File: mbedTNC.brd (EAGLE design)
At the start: 66.7 x 32.9 mm, 58 parts, among them IC1 MKL25ZXXVLH4, IC2 TPS61201, IC3 LMV321-SOT-23-5, J1 MAX5481ETE, J2 SS-7066-NF, Q2 MMBT2222A, Q3 8Mhz, SW3 SPST_TACT-KMR2, U1 BMP180, U2 MCP73831, U3 MAX2659ELT+T, U4 S25FL208K0RMFI013

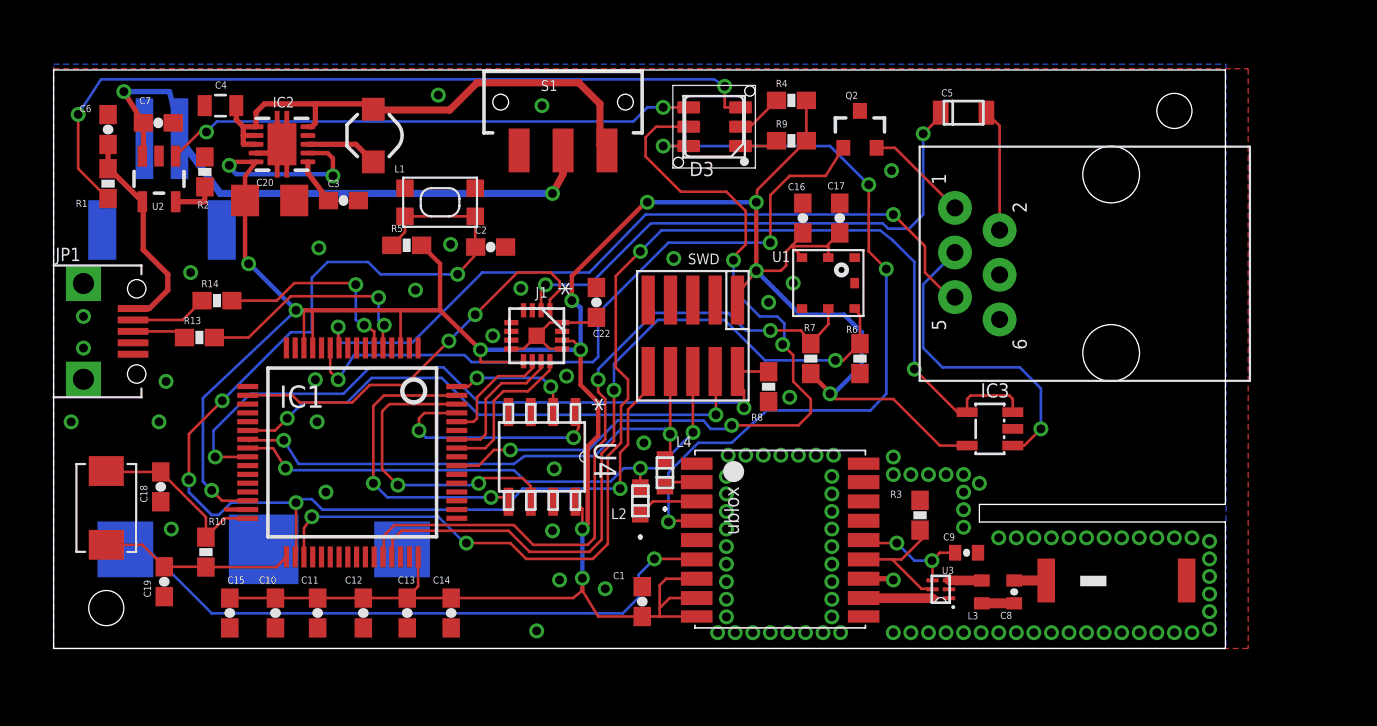
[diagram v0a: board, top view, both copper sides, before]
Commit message: Update
Added support for Yaesu/Icom radios. Moved components around.
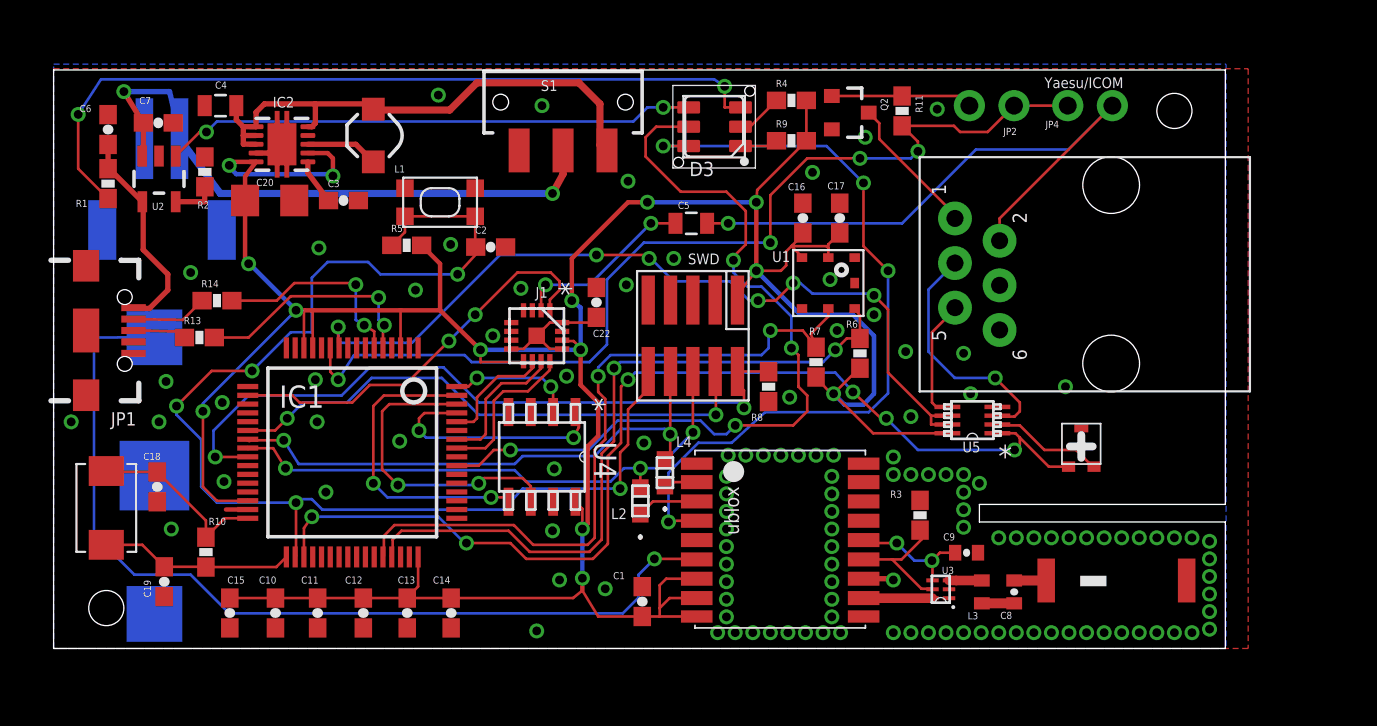
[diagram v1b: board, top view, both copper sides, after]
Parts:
- removed IC3: LMV321-SOT-23-5, dp_devices:SOT-23-5
- added JP2, JP4: JUMPER-PTH-2-NO, SparkFun-Passives:PTH-JUMPER-2-NO_NO_SILK
- added R11: 1K, SparkFun-Resistors:0603-RES
- added U$2: PVA2, wrea:PVA2
- added U5: LMV358, wrea:DDU8-M
- C5: value F921C105MPA -> 10uF; device wrea:PCAP87X53_47N_NIC -> SparkFun-Capacitors:0805
- JP1: value USB-RECEPTABLE -> USB_MICROB_PLUGCONN-11752; device daspilker:FCI-10103594-0001LF -> SparkFun-Connectors:USB-B-MICRO-SMD_V03
- moved C5 16.7 mm to (36.3, 24.2)
- moved BAT1 7.51 mm to (5.74, 9.84), turned to 270 degrees
- moved JP1 1.85 mm to (1.85, 18.1), turned to 0 degrees
- moved Q2 1.17 mm to (45.3, 30.5), turned to 270 degrees
- moved J2 0.60 mm to (58.7, 21.3)
- moved R7 0.36 mm to (43.4, 16.3)
- moved R6 0.30 mm to (45.9, 16.8)
- moved C18 0.20 mm to (5.90, 9.20)
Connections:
- new net N$24: JP2.1, Q2.1, R11.1
- new net N$25: J2.5, U5.5
- new net N$26: U$2.2, U5.2
- net 3.3V: now also U5.8; no longer IC3.5
- net AUDIO_IN: now also U$2.1, U5.1; no longer IC3.3, IC3.4
- net AUDIO_OUT: now also JP4.2
- net CARRIER_IN: now also U5.6, U5.7; no longer J2.5
- net GND: now also JP1.GND1, Q2.2, U$2.3, U5.4; no longer IC3.2, JP1.5, Q2.3
- net N$1: now also JP1.D-1; no longer JP1.2
- net N$18: now also JP1.D+1; no longer JP1.3
- net N$22: now also U5.3; no longer IC3.1
- net N$3: now also Q2.3; no longer Q2.2
- net N$6: now also JP1.VBUS1; no longer JP1.1
- net PTT: now also JP2.2, JP4.1, R11.2; no longer Q2.1
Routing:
- net AUDIO_OUT: track 7.00 -> 36.2 mm, vias 0 -> 1
- net N$21: track 31.2 -> 10.4 mm
- net N$5: track 36.1 -> 52.9 mm
- net PTT: track 40.0 -> 56.7 mm, vias 2 -> 4
- net AUDIO_IN: track 69.8 -> 60.1 mm, vias 4 -> 6
- net N$24: track 0.00 -> 8.06 mm
- net N$25: track 0.00 -> 6.92 mm
- net N$26: track 0.00 -> 6.50 mm
- net N$22: track 18.1 -> 14.0 mm
- net CARRIER_IN: track 43.1 -> 47.0 mm, vias 2 -> 6
- net 3.3V: track 181.0 -> 184.5 mm
- net SDA: track 42.7 -> 40.5 mm
- net N$3: track 5.88 -> 8.05 mm
- net NRESET: track 71.1 -> 71.9 mm
- net GND: vias 109 -> 120
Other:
- board text added: "Yaesu/ICOM"

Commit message: Update
Changed to a 2 circuit digipot. Various other changes
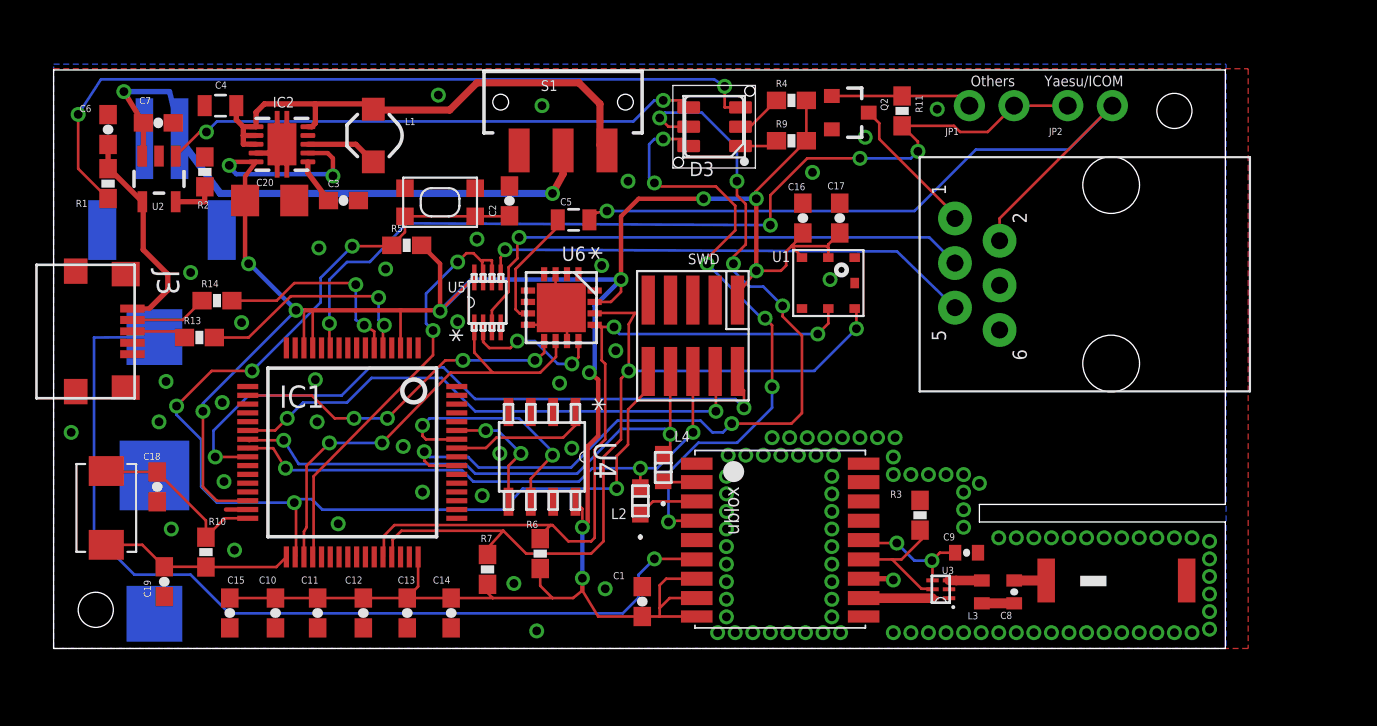
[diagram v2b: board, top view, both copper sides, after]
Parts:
- removed C22: 0.1uF, SparkFun-Capacitors:0603-CAP
- removed J1: MAX5481ETE, wrea:21-0136I_T1633F-3
- removed JP4: JUMPER-PTH-2-NO, SparkFun-Passives:PTH-JUMPER-2-NO_NO_SILK
- removed R8: 10k, SparkFun-Resistors:0603-RES
- removed U$2: PVA2, wrea:PVA2
- added J3: 1981568-1, wrea:CONN_1981568-1
- added U6: MCP4661-XXXX_ML, wrea:QFN16_4X4MC
- JP1: value USB_MICROB_PLUGCONN-11752 -> JUMPER-PTH-2-NO; device SparkFun-Connectors:USB-B-MICRO-SMD_V03 -> SparkFun-Passives:PTH-JUMPER-2-NO_NO_SILK
- R6, R7: value 4.7K -> 2.2k
- moved JP1 53.1 mm to (53.4, 30.9)
- moved U5 28.4 mm to (24.7, 19.7), turned to 90 degrees
- moved R7 22.1 mm to (24.7, 4.50)
- moved R6 21.5 mm to (27.7, 5.40)
- moved C5 6.70 mm to (29.6, 24.4)
- moved JP2 5.60 mm to (59.0, 30.9)
- moved C2 2.84 mm to (25.9, 25.5), turned to 90 degrees
- moved L4 0.32 mm to (34.7, 10.3)
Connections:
- removed net N$19: C22.1, J1.13, J1.16, J1.17, J1.8
- removed net N$26: U$2.2, U5.2
- removed net SPI1_MISO: IC1.64, U4.2
- removed net SPI1_MOSI: IC1.63, U4.5
- removed net SPI1_PCS0: IC1.61, U4.1
- removed net SPI1_SCK: IC1.62, U4.6
- new net P1W: U5.2, U6.6
- net 3.3V: now also U6.15; no longer J1.14, J1.9
- net AUDIO_IN: now also U6.7; no longer U$2.1
- net AUDIO_OUT: now also JP2.2; no longer JP4.2
- net CARRIER_IN: now also IC1.36; no longer IC1.10
- net DAC: now also U6.9; no longer J1.1
- net GND: now also J3.1, U6.10, U6.13, U6.14, U6.17, U6.3, U6.4, U6.5; no longer C22.2, J1.3, JP1.GND1, R8.2, U$2.3
- net N$1: now also J3.4; no longer JP1.D-1
- net N$18: now also J3.3; no longer JP1.D+1
- net N$21: now also U6.8; no longer J1.2
- net N$24: now also JP1.1; no longer JP2.1
- net N$6: now also J3.5; no longer JP1.VBUS1
- net PTT: now also JP1.2, JP2.1; no longer JP2.2, JP4.1
- net SCL: now also R6.1, U6.1; no longer R7.1
- net SDA: now also R7.1, U6.2; no longer R6.1
- net SPI0_MISO: now also U4.2; no longer IC1.60, J1.10
- net SPI0_MOSI: now also U4.5
- net SPI0_PCS0: now also U4.1; no longer J1.12
- net SPI0_SCK: now also U4.6; no longer J1.11
- net TMS: no longer R8.1
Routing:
- net AUDIO_IN: track 60.1 -> 25.9 mm, vias 6 -> 2
- net CARRIER_IN: track 47.0 -> 24.9 mm, vias 6 -> 2
- net N$25: track 6.92 -> 28.5 mm, vias 0 -> 1
- net 3.3V: track 184.5 -> 163.9 mm, vias 14 -> 13
- net SPI1_SCK: track 17.8 -> 0.00 mm, vias 2 -> 0
- net SPI1_MOSI: track 17.5 -> 0.00 mm, vias 2 -> 0
- net N$22: track 14.0 -> 31.1 mm
- net SPI1_PCS0: track 13.5 -> 0.00 mm, vias 2 -> 0
- net GPS_LED: track 45.0 -> 35.7 mm, vias 4 -> 6
- net P1W: track 0.00 -> 8.18 mm, vias 0 -> 2
- net N$19: track 7.53 -> 0.00 mm
- net SPI1_MISO: track 7.26 -> 0.00 mm, vias 2 -> 0
- net SPI0_MOSI: track 0.00 -> 7.23 mm, vias 0 -> 2
- net SDA: track 40.5 -> 47.3 mm
- net SPI0_MISO: track 6.67 -> 0.00 mm
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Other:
- board text added: "Others"

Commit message: Update.
Move to 4 layer board. New LNA with internal switch for an active
external ant. Finalizing parts, moved stuff around.
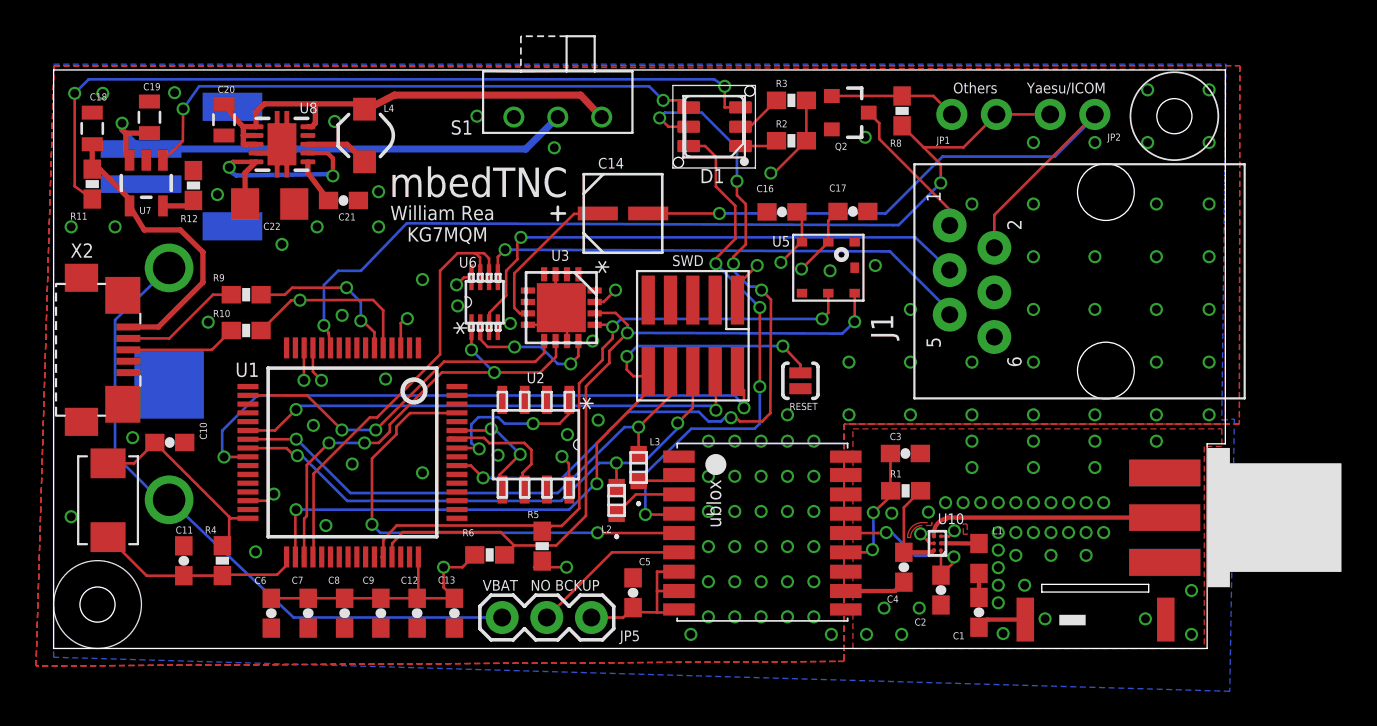
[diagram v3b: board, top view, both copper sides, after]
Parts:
- removed BAT1: (no value), SparkFun-Electromechanical:BATTCON_12MM
- removed C15: 1.0uF, SparkFun-Capacitors:0603-CAP
- removed IC1: MKL25ZXXVLH4, wrea:64-LQFP
- removed J2: SS-7066-NF, wrea:SS-7066-NF
- removed J3: 1981568-1, wrea:CONN_1981568-1
- removed JP3: LiPo Battery, SparkFun:JST-2-SMD
- removed Q3: 8Mhz, wibauxl:CRYSTAL_5X3.2
- removed R13, R14: 33, SparkFun-Resistors:0603-RES
- removed R7: 2.2k, SparkFun-Passives:0603-RES
- removed SW3: SPST_TACT-KMR2, adafruit:KMR2
- removed U$4: AF816M157502-T, wrea:AF816
- removed U4: S25FL208K0RMFI013, wrea:SO-8_SOA008
- added BATT1: BK-890, wrea:BATTCON_12MMPC
- added C21: 1uF, SparkFun-Capacitors:0603-CAP
- added C22: 22uF, SparkFun-Capacitors:1206
- added J1: SS-7066-NF, wrea:SS-7066-NF
- added JP4: LiPo Battery, SparkFun:JST-2-SMD
- added JP5: PTH-JUMPER-3-NO, wrea:PTH-JUMPER-3-NO
- added Q1: 8Mhz, wibauxl:CRYSTAL_5X3.2
- added R12, R8: 1K, SparkFun-Resistors:0603-RES
- added RESET: JUMPER-PAD-2-NOYES_SILK, SparkFun-Passives:PAD-JUMPER-2-NO_YES_SILK
- added U$2: VLP-ZZZ-X, wrea:VLP-ZZZ-X
- added U10: MAX2674EWT+T, wrea:21-0217D_W61B1-1
- added U7: MCP73831, SparkFun:SOT23-5
- added X1: SMA003.062, wrea:SMA003.062
- added X2: MICRO-USB-ZX62R-B-5P, con-hirose:ZX62R-B-5P
- C1: value 0.1uF -> 100pF; device SparkFun:0603-CAP -> SparkFun-Capacitors:0603-CAP
- C10, C11: value 1.0uF -> 22pF
- C14: value 0.1uF -> UWX1C100MCL2GB; device SparkFun-Capacitors:0603-CAP -> wrea:PCAP_4X5.4-ELECT
- C18, C19: value 22pF -> 4.7uF; device SparkFun-Capacitors:0603-CAP -> SparkFun-Capacitors:0805
- C2: value 1.0uF -> 10pF
- C20: value 22uF -> 10uF; device SparkFun-Capacitors:1206 -> SparkFun-Capacitors:0805
- C3: value 0.1uF -> 39pF
- C4: value 10uF -> 100pF; device SparkFun-Capacitors:0805 -> SparkFun-Capacitors:0603-CAP
- C5: value 10uF -> 0.1uF; device SparkFun-Capacitors:0805 -> SparkFun:0603-CAP
- C6, C7: value 4.7uF -> 1.0uF
- C8: value 470pF -> 1.0uF; device SparkFun:0402-CAP -> SparkFun-Capacitors:0603-CAP
- C9: value 33nF -> 0.1uF; device SparkFun:0402-CAP -> SparkFun-Capacitors:0603-CAP
- L1: value 4.7uH, 1.2A -> 91nH; device SparkFun-Passives:CDRH2D09 -> SparkFun-Passives:0603
- L3: value 6.8nH -> BLM18HG102SN1D; device SparkFun:C0402 -> wrea:IND_BLM18_0603
- L4: value BLM18HG102SN1D -> 4.7uH, 1.2A; device wrea:IND_BLM18_0603 -> SparkFun-Passives:CDRH2D09
- R1: value 82 -> 25.5k
- R10: value 1M -> 33
- R11: value 1K -> 82
- R2: value 1K -> 15
- R3: value 10k -> 5.6
- R4: value 5.6 -> 1M
- R5: value 10k -> 2.2k; device SparkFun-Resistors:0603-RES -> SparkFun-Passives:0603-RES
- R9: value 15 -> 33
- S1: value (none) -> EG1270; device SparkFun-Electromechanical:SWITCH-SPDT-SMD -> wrea:EG1270
- U$1: value VLP-ZZZ-X -> AF816M157502-T; device wrea:VLP-ZZZ-X -> wrea:AF816
- U1: value BMP180 -> MKL25ZXXVLH4; device SparkFun-Sensors:BMP180 -> wrea:64-LQFP
- U2: value MCP73831 -> S25FL208K0RMFI013; device SparkFun:SOT23-5 -> wrea:SO-8_SOA008
- U3: value MAX2659ELT+T -> MCP4661-XXXX_ML; device wrea:DFN-6 -> wrea:QFN16_4X4MC
- U5: value LMV358 -> BMP180; device wrea:DDU8-M -> SparkFun-Sensors:BMP180
- U6: value MCP4661-XXXX_ML -> LMV358; device wrea:QFN16_4X4MC -> wrea:DDU8-M
- moved R1 48.7 mm to (48.5, 8.97), turned to 0 degrees
- moved C4 46.9 mm to (48.4, 4.62), turned to 270 degrees
- moved R11 46.3 mm to (2.20, 26.4), turned to 90 degrees
- moved L1 42.0 mm to (52.7, 5.12)
- moved R4 41.7 mm to (9.61, 5.00), turned to 270 degrees
- moved C8 38.1 mm to (16.6, 2.01)
- moved U$1 35.5 mm to (59.3, 1.65), turned to 0 degrees
- moved C3 35.1 mm to (48.5, 11.1)
- moved C9 33.5 mm to (18.6, 2.01), turned to 270 degrees
- moved R2 33.4 mm to (42.0, 28.9), turned to 0 degrees
- moved C2 33.1 mm to (50.5, 3.33), turned to 270 degrees
- moved R9 32.3 mm to (11.0, 20.1)
- moved C7 29.2 mm to (14.5, 2.01), turned to 270 degrees
- moved C6 29.1 mm to (12.4, 2.01), turned to 270 degrees
- moved U1 28.8 mm to (17.0, 11.2), turned to 270 degrees
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- renumbered D3 to D1, IC2 to U8
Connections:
- removed net N$14: C9.2, U$3.14_VCC_RF, U3.4
- removed net N$9: C8.2, L3.1
- new net GPS_INT: U$3.5_EXTINT0, U1.61
- new net N$19: C1.1, L1.1
- new net N$26: U10.C2, X1.RF
- new net N$27: C3.1, R1.1, U$3.13_ANTON
- new net N$28: BATT1.C2, BATT1.C3, JP5.3
- new net N2: C4.2, U$3.11_RF_IN
- net 3.3V: now also C22.1, C5.1, C6.1, C7.1, C8.1, C9.1, JP5.1, R2.2, R3.2, U1.13, U1.14, U1.30, U1.48, U2.8, U3.15, U5.2, U5.3, U6.8; no longer C1.1, C10.1, C11.1, C14.1, C15.1, C20.1, IC1.13, IC1.14, IC1.3, IC1.30, IC1.48, R4.2, R7.2, R9.2, U1.2, U4.8, U5.8, U6.15
- net AUDIO_IN: now also U1.35, U3.7, U6.1; no longer IC1.35, U5.1, U6.7
- net AUDIO_OUT: now also C14.2, J1.2; no longer C5.2, J2.2
- net CARRIER_IN: now also U1.36, U6.6, U6.7; no longer IC1.36, U5.6, U5.7
- net CRG_LED_AN: now also R11.1; no longer R1.1
- net CRG_LED_CATH: now also U7.1; no longer U2.1
- net D+: now also R10.2, U1.5; no longer IC1.5, R13.2
- net D-: now also R9.2, U1.6; no longer IC1.6, R14.2
- net DAC: now also U1.18, U3.9; no longer IC1.18, U6.9
- net GND: now also BATT1.C1, C10.1, C11.1, C18.2, C19.2, C21.2, C22.2, C5.2, C8.2, C9.2, J1.6, JP4.1, R12.2, RESET.1, U1.15, U1.16, U1.31, U1.4, U1.47, U10.B2, U10.C1, U2.4, U3.10, U3.13, U3.14, U3.17, U3.3, U3.4, U3.5, U5.7, U7.2, X1.C2, X1.C3, X1.C4, X1.C5, X2.1; no longer BAT1.GND, C1.2, C10.2, C11.2, C14.2, C15.2, C18.1, C19.1, C4.2, C9.1, IC1.15, IC1.16, IC1.31, IC1.4, IC1.47, J2.6, J3.1, JP3.1, R2.2, R3.1, SW3.2, SW3.4, U1.7, U2.2, U3.1, U3.2, U4.4, U5.4, U6.10, U6.13, U6.14, U6.17, U6.3, U6.5
- net N$1: now also R9.1, X2.4; no longer J3.4, R14.1
- net N$10: now also L4.P$1; no longer L1.P$1
- net N$11: now also C10.2, Q1.2, R4.1, U1.32; no longer C18.2, IC1.32, Q3.2, R10.1
- net N$12: now also C1.2, U$1.FEED; no longer C8.1, U$4.FEED
- net N$13: now also C11.2, Q1.1, R4.2, U1.33; no longer C19.2, IC1.33, Q3.1, R10.2
- net N$15: now also R3.1; no longer R4.1
- net N$16: now also U1.56; no longer IC1.56
- net N$17: now also R2.1; no longer R9.1
- net N$18: now also R10.1, X2.3; no longer J3.3, R13.1
- net N$2: now also C4.1, R1.2, U10.A2; no longer U$3.11_RF_IN, U3.6
- net N$21: now also C14.1, U3.8; no longer C5.1, U6.8
- net N$22: now also J1.3, U6.3; no longer J2.3, U5.3
- net N$23: now also L3.2; no longer L4.2
- net N$24: now also R8.1; no longer R11.1
- net N$25: now also J1.5, U6.5; no longer J2.5, U5.5
- net N$3: now also J1.1; no longer J2.1
- net N$4: now also L1.2, U10.B1; no longer R3.2, U$3.13_ANTON, U3.5
- net N$5: now also JP5.2; no longer BAT1.PWR@1
- net N$6: now also C18.1, R11.2, U7.4, X2.5; no longer C6.1, J3.5, R1.2, U2.4
- net N$7: now also C19.1, JP4.2, S1.P$2, U7.3; no longer C7.1, JP3.2, S1.2, U2.3
- net N$8: now also C2.1, U$3.14_VCC_RF, U10.A1; no longer L3.2, U3.3
- net NRESET: now also RESET.2, U1.34; no longer C2.1, IC1.34, R5.1, SW3.1, SW3.3
- net P1W: now also U3.6, U6.2; no longer U5.2, U6.6
- net PROG1: now also R12.1, U7.5; no longer R2.1, U2.5
- net PTT: now also R8.2, U1.11; no longer IC1.11, R11.2
- net RX_0: now also L3.1, U1.23; no longer IC1.23, L4.1
- net SCL: now also R5.1, U1.44, U3.1, U5.5; no longer IC1.44, R6.1, U1.5, U6.1
- net SDA: now also R6.1, U1.45, U3.2, U5.6; no longer IC1.45, R7.1, U1.6, U6.2
- net SPI0_MISO: now also U2.2; no longer U4.2
- net SPI0_MOSI: now also U1.59, U2.5; no longer IC1.59, U4.5
- net SPI0_PCS0: now also U1.57, U2.1; no longer IC1.57, U4.1
- net SPI0_SCK: now also U1.58, U2.6; no longer IC1.58, U4.6
- net TCK: now also U1.22; no longer IC1.22
- net TMS: now also U1.25; no longer IC1.25
- net TX_0: now also U1.24; no longer IC1.24
- net TX_LED: now also U1.55; no longer IC1.55
- net VAUX: now also C21.1; no longer C3.1
- net VIN: now also C20.1, L4.P$2, S1.P$3; no longer C4.1, L1.P$2, S1.3
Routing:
- net 3.3V: track 163.9 -> 70.2 mm, vias 13 -> 15
- net N$5: track 52.9 -> 9.06 mm, vias 1 -> 0
- net N$28: track 0.00 -> 37.7 mm
- net GPS_INT: track 0.00 -> 27.6 mm, vias 0 -> 2
- net NRESET: track 65.4 -> 41.4 mm, vias 5 -> 4
- net N$26: track 0.00 -> 13.7 mm
- net N$8: track 1.87 -> 9.50 mm, vias 0 -> 2
- net N$27: track 0.00 -> 7.51 mm, vias 0 -> 2
- net N$14: track 7.02 -> 0.00 mm, vias 2 -> 0
- net N$7: track 36.8 -> 30.0 mm, vias 2 -> 1
- net TX_LED: track 51.1 -> 44.3 mm
- net SPI0_SCK: track 14.3 -> 7.88 mm, vias 2 -> 0
- net N$6: track 12.2 -> 17.7 mm
- net N$4: track 7.33 -> 2.16 mm
- net AUDIO_OUT: track 42.8 -> 37.8 mm
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- added copper zone on layer 15, net 3.3V
- added copper zone on layer 2, net GND
- added copper zone on layer 1, net N$14
- added copper zone on layer 1, net N$9
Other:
- outline, holes or cut-outs redrawn
- board text added: "VBAT NO BCKUP"
- board text added: "William Rea KG7MQM"
- board text added: "mbedTNC"

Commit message: Update
Moved some components around to accommodate case design
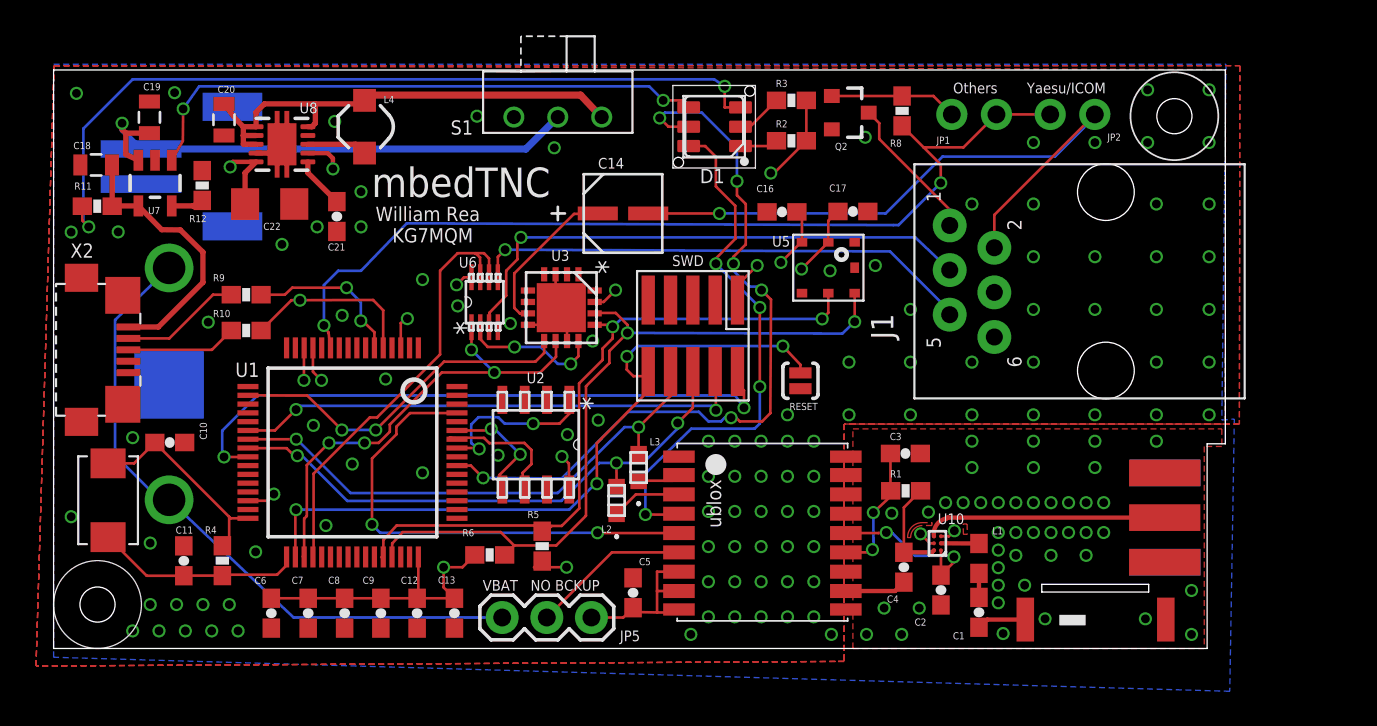
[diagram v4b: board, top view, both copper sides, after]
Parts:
- moved C18 2.09 mm to (2.42, 27.5), turned to 180 degrees
- moved R11 1.29 mm to (2.48, 25.2), turned to 0 degrees
- moved C21 0.99 mm to (16.1, 24.6), turned to 270 degrees
- moved R12 0.50 mm to (8.46, 26.4)
- moved L4 0.50 mm to (17.7, 29.7)
- moved U7 0.50 mm to (5.78, 26.5)
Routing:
- net 3.3V: track 70.2 -> 63.6 mm
- net N$6: track 17.7 -> 15.6 mm
- net CRG_LED_AN: track 46.1 -> 46.9 mm
- net GND: vias 142 -> 151
